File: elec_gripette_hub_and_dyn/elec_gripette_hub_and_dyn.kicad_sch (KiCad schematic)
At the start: 10 parts

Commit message: [update] sch reviewed by Claude
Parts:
- H4: value Mounting Holes M2,5 -> M2,5 x 4mm spacer; footprint MountingHole:MountingHole_2.7mm_M2.5_ISO7380_Pad_TopBottom -> LCSC_parts_lib:SMD_BD5.6-D4.1_spacer; LCSC Part (none) -> C2916324
- H5, H6, H7: value Mounting Holes M2 -> M2,5 x 4mm spacer; footprint MountingHole:MountingHole_2.7mm_M2.5_ISO7380_Pad_TopBottom -> LCSC_parts_lib:SMD_BD5.6-D4.1_spacer; LCSC Part (none) -> C2916324
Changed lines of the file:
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@@
 	(polyline
 		(pts
-			(xy 40.64 124.46) (xy 64.77 124.46)
+			(xy 40.64 124.46) (xy 46.99 124.46)
 		)
 		(stroke
@@
 	(polyline
 		(pts
+			(xy 40.64 139.7) (xy 40.64 142.24)
+		)
+		(stroke
+			(width 0)
+			(type default)
+		)
+	)
+	(polyline
+		(pts
 			(xy 91.44 35.56) (xy 91.44 60.96)
 		)
@@
 		)
 	)
+	(polyline
+		(pts
+			(xy 58.42 140.97) (xy 64.77 140.97)
+		)
+		(stroke
+			(width 0)
+			(type default)
+		)
+	)
 	(wire
 		(pts
@@
 		)
 	)
+	(polyline
+		(pts
+			(xy 55.88 124.46) (xy 57.15 124.46)
+		)
+		(stroke
+			(width 0)
+			(type default)
+		)
+	)
 	(wire
 		(pts
@@
 	(polyline
 		(pts
-			(xy 130.81 144.78) (xy 130.81 146.05)
+			(xy 50.8 124.46) (xy 52.07 124.46)
 		)
 		(stroke
@@
 		)
 	)
-	(wire
+	(polyline
 		(pts
-			(xy 129.54 175.26) (xy 129.54 176.53)
+			(xy 53.34 124.46) (xy 54.61 124.46)
 		)
 		(stroke
@@
 	(polyline
 		(pts
-			(xy 129.54 144.78) (xy 154.94 144.78)
+			(xy 48.26 140.97) (xy 49.53 140.97)
 		)
 		(stroke
@@
 	(polyline
 		(pts
-			(xy 64.77 139.7) (xy 64.77 142.24)
+			(xy 130.81 144.78) (xy 130.81 146.05)
+		)
+		(stroke
+			(width 0)
+			(type default)
+		)
+	)
+	(wire
+		(pts
+			(xy 129.54 175.26) (xy 129.54 176.53)
 		)
 		(stroke
@@
 	(polyline
 		(pts
-			(xy 40.64 140.97) (xy 64.77 140.97)
+			(xy 129.54 144.78) (xy 154.94 144.78)
+		)
+		(stroke
+			(width 0)
+			(type default)
+		)
+	)
+	(polyline
+		(pts
+			(xy 50.8 140.97) (xy 52.07 140.97)
 		)
 		(stroke
@@
 	(polyline
 		(pts
+			(xy 40.64 140.97) (xy 46.99 140.97)
+		)
+		(stroke
+			(width 0)
+			(type default)
+		)
+	)
+	(polyline
+		(pts
 			(xy 38.1 116.84) (xy 27.94 116.84)
 		)
@@
 		)
 	)
+	(polyline
+		(pts
+			(xy 53.34 140.97) (xy 54.61 140.97)
+		)
+		(stroke
+			(width 0)
+			(type default)
+		)
+	)
 	(wire
 		(pts
@@
 	(polyline
 		(pts
+			(xy 55.88 140.97) (xy 57.15 140.97)
+		)
+		(stroke
+			(width 0)
+			(type default)
+		)
+	)
+	(polyline
+		(pts
 			(xy 154.94 116.84) (xy 129.54 116.84)
 		)
@@
 	(polyline
 		(pts
-			(xy 129.54 104.14) (xy 147.32 104.14)
+			(xy 64.77 139.7) (xy 64.77 142.24)
 		)
 		(stroke
@@
 	(polyline
 		(pts
-			(xy 40.64 139.7) (xy 40.64 142.24)
+			(xy 58.42 124.46) (xy 64.77 124.46)
+		)
+		(stroke
+			(width 0)
+			(type default)
+		)
+	)
+	(polyline
+		(pts
+			(xy 48.26 124.46) (xy 49.53 124.46)
+		)
+		(stroke
+			(width 0)
+			(type default)
+		)
+	)
+	(polyline
+		(pts
+			(xy 129.54 104.14) (xy 147.32 104.14)
 		)
 		(stroke
@@
 			)
 		)
-		(property "Value" "Mounting Holes M2"
+		(property "Value" "M2,5 x 4mm spacer"
 			(at 125.73 166.37 0)
 			(effects
@@
 			)
 		)
-		(property "Footprint" "MountingHole:MountingHole_2.7mm_M2.5_ISO7380_Pad_TopBottom"
+		(property "Footprint" "LCSC_parts_lib:SMD_BD5.6-D4.1_spacer"
 			(at 119.38 172.72 0)
 			(effects
@@
 			)
 		)
+		(property "LCSC Part" "C2916324"
+			(at 119.38 172.72 0)
+			(effects
+				(font
+					(size 1.27 1.27)
+				)
+				(hide yes)
+			)
+		)
 		(pin "1"
 		)
@@
 			)
 		)
-		(property "Value" "Mounting Holes M2"
+		(property "Value" "M2,5 x 4mm spacer"
 			(at 117.856 166.116 0)
 			(effects
@@
 			)
 		)
-		(property "Footprint" "MountingHole:MountingHole_2.7mm_M2.5_ISO7380_Pad_TopBottom"
+		(property "Footprint" "LCSC_parts_lib:SMD_BD5.6-D4.1_spacer"
 			(at 124.46 172.72 0)
 			(effects
@@
 			)
 		)
+		(property "LCSC Part" "C2916324"
+			(at 124.46 172.72 0)
+			(effects
+				(font
+					(size 1.27 1.27)
+				)
+				(hide yes)
+			)
+		)
 		(pin "1"
 		)
@@
 			)
 		)
-		(property "Value" "Mounting Holes M2,5"
+		(property "Value" "M2,5 x 4mm spacer"
 			(at 112.268 166.37 0)
 			(effects
@@
 			)
 		)
-		(property "Footprint" "MountingHole:MountingHole_2.7mm_M2.5_ISO7380_Pad_TopBottom"
+		(property "Footprint" "LCSC_parts_lib:SMD_BD5.6-D4.1_spacer"
 			(at 114.3 172.72 0)
 			(effects
@@
 			)
 		)
+		(property "LCSC Part" "C2916324"
+			(at 114.3 172.72 0)
+			(effects
+				(font
+					(size 1.27 1.27)
+				)
+				(hide yes)
+			)
+		)
 		(pin "1"
 		)
@@
 			)
 		)
-		(property "Value" "Mounting Holes M2"
+		(property "Value" "M2,5 x 4mm spacer"
 			(at 135.89 166.37 0)
 			(effects
@@
 			)
 		)
-		(property "Footprint" "MountingHole:MountingHole_2.7mm_M2.5_ISO7380_Pad_TopBottom"
+		(property "Footprint" "LCSC_parts_lib:SMD_BD5.6-D4.1_spacer"
 			(at 129.54 172.72 0)
 			(effects
@@
 			(at 129.54 172.72 0)
 			(effects
+				(font
+					(size 1.27 1.27)
+				)
+				(hide yes)
+			)
+		)
+		(property "LCSC Part" "C2916324"
+			(at 129.54 172.72 0)
+			(effects

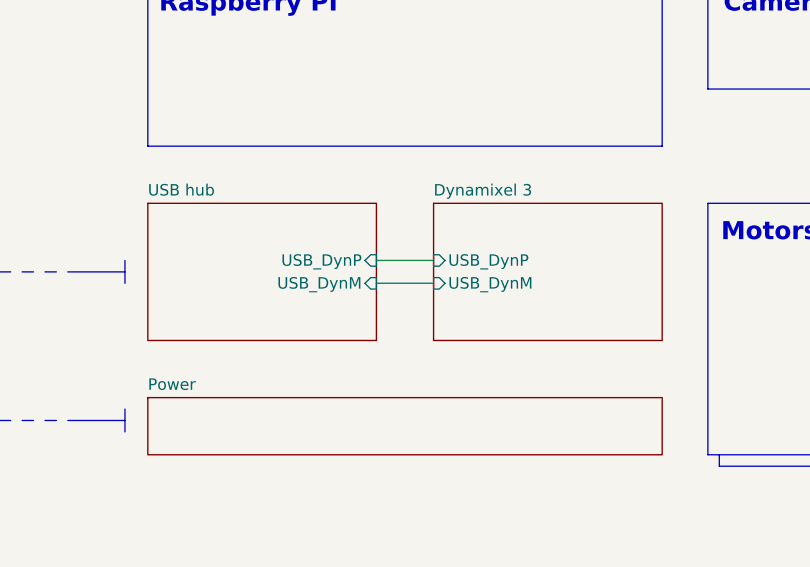
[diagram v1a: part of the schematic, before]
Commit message: [update] Gripette hub routed
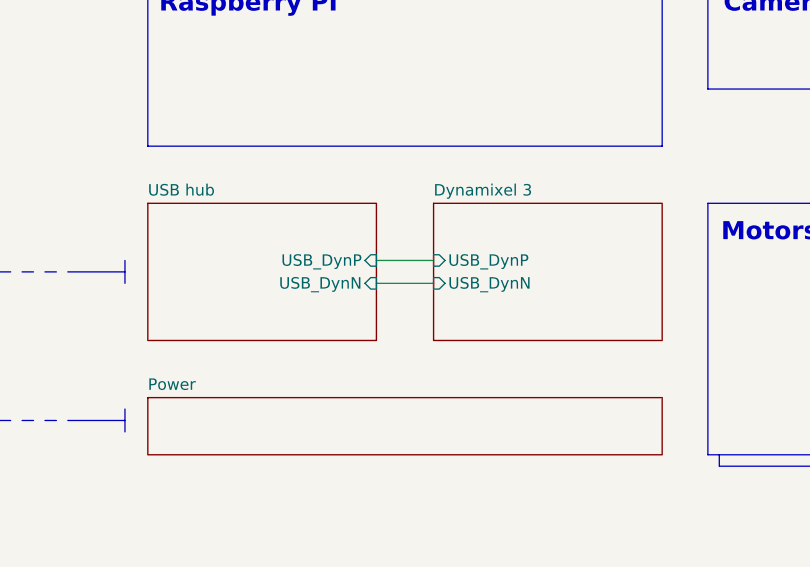
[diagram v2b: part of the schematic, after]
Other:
- sheet Dynamixel 3 ports: added USB_DynN; removed USB_DynM
- sheet USB hub ports: added USB_DynN; removed USB_DynM
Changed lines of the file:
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@@
 			)
 		)
-		(property "Description" "Mounting Hole"
+		(property "Description" "Mounting Hole with connection"
 			(at 119.38 172.72 0)
 			(effects
@@
 			)
 		)
-		(property "Description" "Mounting Holes M2,5"
+		(property "Description" "Mounting Hole with connection"
 			(at 128.27 166.624 0)
 			(effects
@@
 			)
 		)
-		(property "Description" "Mounting Holes M2,5"
+		(property "Description" "Mounting Hole with connection"
 			(at 118.11 166.624 0)
 			(effects
@@
 			)
 		)
-		(property "Description" "Mounting Hole"
+		(property "Description" "Mounting Hole with connection"
 			(at 129.54 172.72 0)
 			(effects
@@
 			)
 		)
-		(pin "USB_DynM" input
+		(pin "USB_DynN" input
 			(at 92.71 125.73 0)
 			(effects
@@
 			)
 		)
-		(pin "USB_DynM" input
+		(pin "USB_DynN" input
 			(at 99.06 125.73 180)
 			(effects

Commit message: [uptate] Gripette hub ok for JLC
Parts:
- H1: value PCB0xyz -> PCB01200
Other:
- note added: ""elec_hub_and_dyn" is a part of the Grabette/Gripette project, it is a under-HAT for rasp zero 2w with a USB hub and a Dynamixel device."
- note added: "16/04/2026"
- note added: "ASE01201"
- note removed: ""elec_hub_and_dyn" is a part of the Grabette/Gripette project, it is a under-HAT for rasp 2w with a USB hub and a Dynamixel device."
- note removed: "ASE0xyz"
- note removed: "dd/mm/2026"
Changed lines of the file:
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@@
 	(title_block
 		(title "Grippette - USB hub and Dynamixel device")
-		(date "2026-04-07")
+		(date "2026-04-16")
 		(rev "A1")
 		(company "Pollen Robotics/HF")
@@
 		)
 	)
-	(text "ASE0xyz"
+	(text "ASE01201"
 		(exclude_from_sim no)
 		(at 38.1 173.355 0)
@@
 		)
 	)
-	(text "\"elec_hub_and_dyn\" is a part of the Grabette/Gripette project, it is a \nunder-HAT for rasp 2w with a USB hub and a Dynamixel device."
+	(text "\"elec_hub_and_dyn\" is a part of the Grabette/Gripette project, it is a \nunder-HAT for rasp zero 2w with a USB hub and a Dynamixel device."
 		(exclude_from_sim no)
 		(at 19.304 27.686 0)
@@
 		)
 	)
-	(text "dd/mm/2026"
+	(text "16/04/2026"
 		(exclude_from_sim no)
 		(at 39.37 44.45 0)
@@
 			)
 		)
-		(property "Value" "PCB0xyz"
+		(property "Value" "PCB01200"
 			(at 38.1 169.545 0)
 			(effects

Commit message: [update] Release A1, small batch @JLC
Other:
- note added: "Supplying the motors: - through Vbatt (from the XT60): R28 must be populated - through Dxl: R28 must be removed. Motor communication: - USB (Dynamixel-TTL converter): R15 must be populated - Dynamixel: R15 must be removed."
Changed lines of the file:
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@@
+		)
+	)
+	(text "Supplying the motors:\n- through Vbatt (from the XT60): R28 must be populated\n- through Dxl: R28 must be removed.\n\nMotor communication:\n- USB (Dynamixel-TTL converter): R15 must be populated\n- Dynamixel: R15 must be removed."
+		(exclude_from_sim no)
+		(at 167.132 122.682 0)
+		(effects
+			(font
+				(size 2.0066 2.0066)
+			)
+			(justify left bottom)
 		)
 	)
@@
 	(text "- SO10x: USB connector + Dynamixel/Feetech @7,4V\n- OpenArm: USB connector + 24V on XT60"
 		(exclude_from_sim no)
-		(at 166.878 93.98 0)
+		(at 166.116 92.964 0)
 		(effects
 			(font

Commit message: [update] Added error to gripette, going to B1
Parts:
- H2: now left out of the parts list
- H4, H5, H6, H7: now in the parts list
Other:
- note added: "ToDo: - Spacers are Excluded from the BoM! - EN pin should not exceed 6V - pogo-pins of USB pair are too high (should be 3mm) - xtra gnd pogo (or closer one) - USB pair pads are shifted of 1 mm in Y (should be 1,92 mm) - DCDC 5V should be wired on Vbus (on A1 hot-plugging motors: short circuit) - DXL/Feetech compat (DIP switch + MOS?) - reseting usb hub - add jumper for accessing uart-dynamixel f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"
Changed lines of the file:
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@@
 		)
 	)
+	(text "ToDo:\n - Spacers are Excluded from the BoM!\n - EN pin should not exceed 6V\n - pogo-pins of USB pair are too high (should be 3mm)\n - xtra gnd pogo (or closer one)\n - USB pair pads are shifted of 1 mm in Y (should be 1,92 mm)\n - DCDC 5V should be wired on Vbus (on A1 hot-plugging motors: short circuit)\n - DXL/Feetech compat (DIP switch + MOS?)\n - reseting usb hub\n - add jumper for accessing uart-dynamixel from rasp-uart\n - fix led colors, should be 4xgreen + 1 red\n - add uart for terminal?"
+		(exclude_from_sim no)
+		(at 44.958 126.238 0)
+		(effects
+			(font
+				(size 3 3)
+				(thickness 0.6)
+				(bold yes)
+				(italic yes)
+			)
+			(justify left bottom)
+		)
+	)
 	(text "SN"
 		(exclude_from_sim no)
@@
 		(unit 1)
 		(exclude_from_sim no)
-		(in_bom no)
+		(in_bom yes)
 		(on_board yes)
 		(dnp no)
@@
 		(unit 1)
 		(exclude_from_sim no)
-		(in_bom no)
+		(in_bom yes)
 		(on_board yes)
 		(dnp no)
@@
 		(unit 1)
 		(exclude_from_sim no)
-		(in_bom no)
+		(in_bom yes)
 		(on_board yes)
 		(dnp no)
@@
 		(unit 1)
 		(exclude_from_sim no)
-		(in_bom no)
+		(in_bom yes)
 		(on_board yes)
 		(dnp no)
@@
 		(unit 1)
 		(exclude_from_sim no)
-		(in_bom yes)
+		(in_bom no)
 		(on_board yes)
 		(dnp no)

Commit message: [update] SCH B1-RC1
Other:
- sheet Dynamixel 3 renamed Dynamixel-TTL over USB
- added sheet Dynamixel-TTL (dynamixel_3_from_rasp.kicad_sch)
- sheet Dynamixel-TTL over USB ports: added Dyn_data; removed none
- note added: "B1"
- note added: "ToDo: - DXL/Feetech compat (DIP switch + MOS?) - add jumper for accessing uart-dynamixel from rasp-uart"
- note added: "[fix] Spacers in the BoM [fix] DCDC is now 5A capable [fix] USB pogo-pins position [update] 5V DCDC is on Vbus [update] 4 mm spacers/pogo-pins [added] Test points + access to UART-Dynamixel [added] Hub reset rasp-accessible"
- note added: "dd/mm/2026"
- note removed: "ToDo: - Spacers are Excluded from the BoM! - EN pin should not exceed 6V - pogo-pins of USB pair are too high (should be 3mm) - xtra gnd pogo (or closer one) - USB pair pads are shifted of 1 mm in Y (should be 1,92 mm) - DCDC 5V should be wired on Vbus (on A1 hot-plugging motors: short circuit) - DXL/Feetech compat (DIP switch + MOS?) - reseting usb hub - add jumper for accessing uart-dynamixel f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"
